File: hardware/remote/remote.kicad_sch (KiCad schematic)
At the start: 27 parts

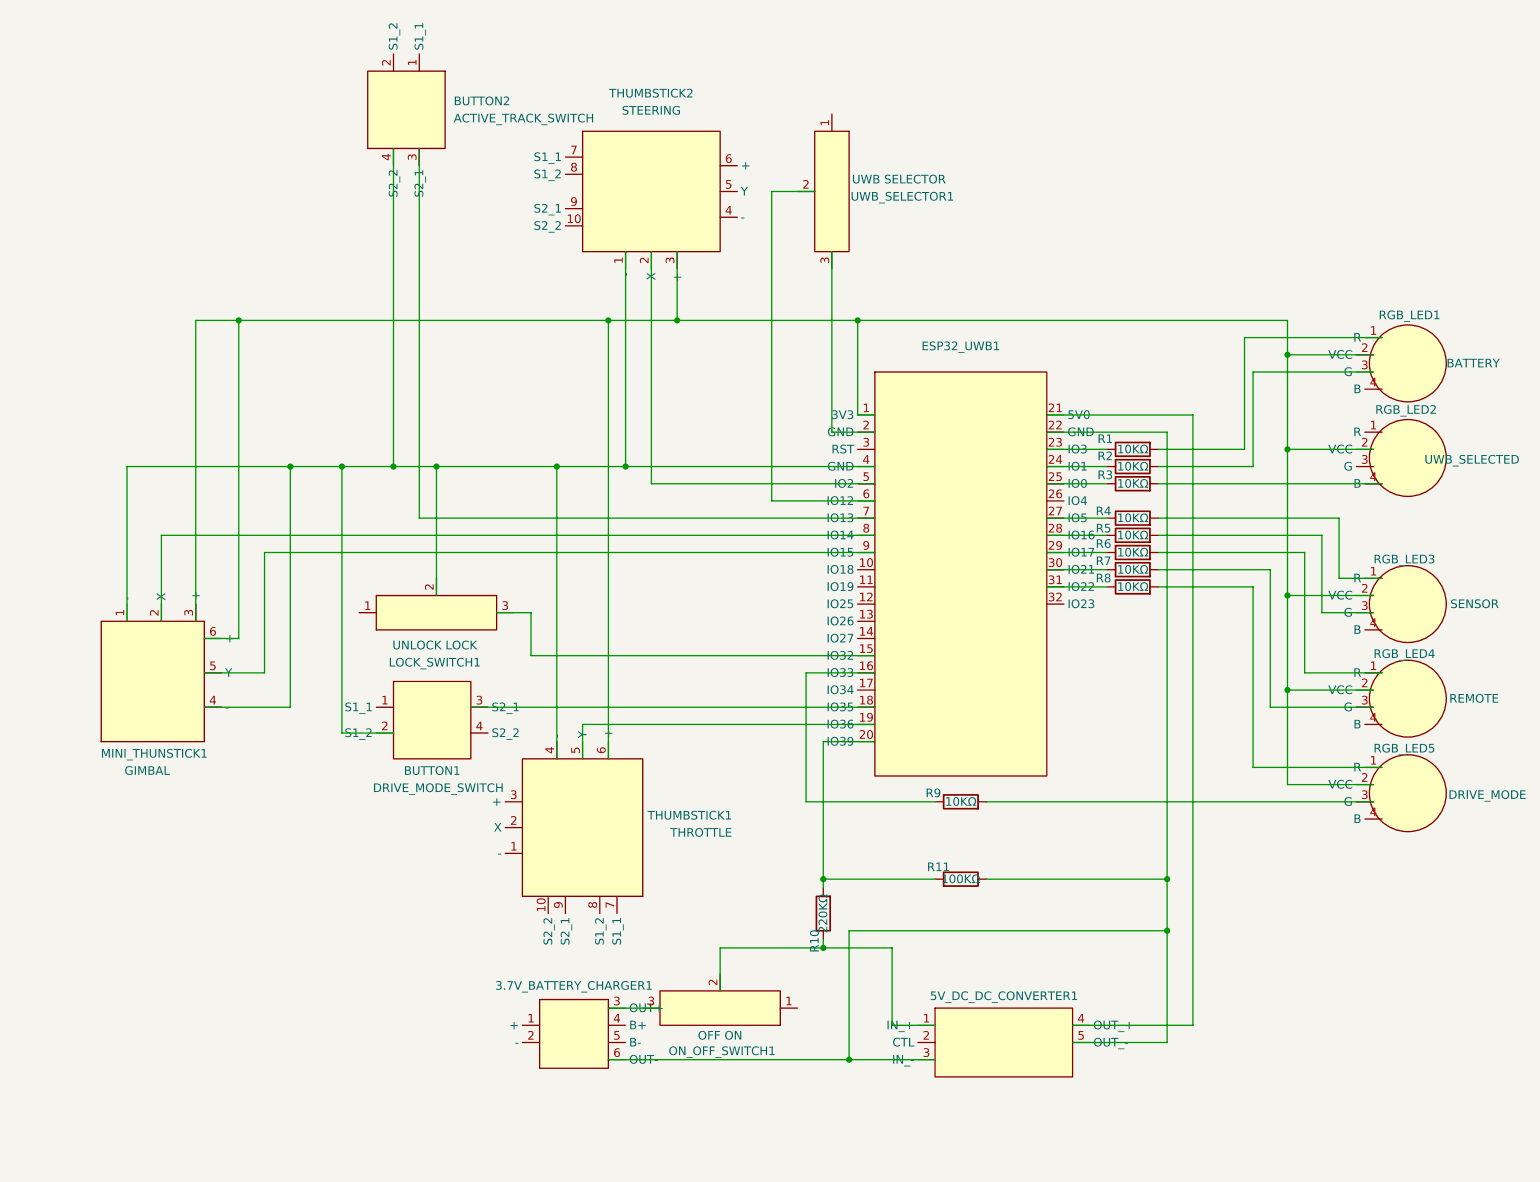
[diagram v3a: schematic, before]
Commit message: hardware: Reroute the wires to fix unavailable PINs.
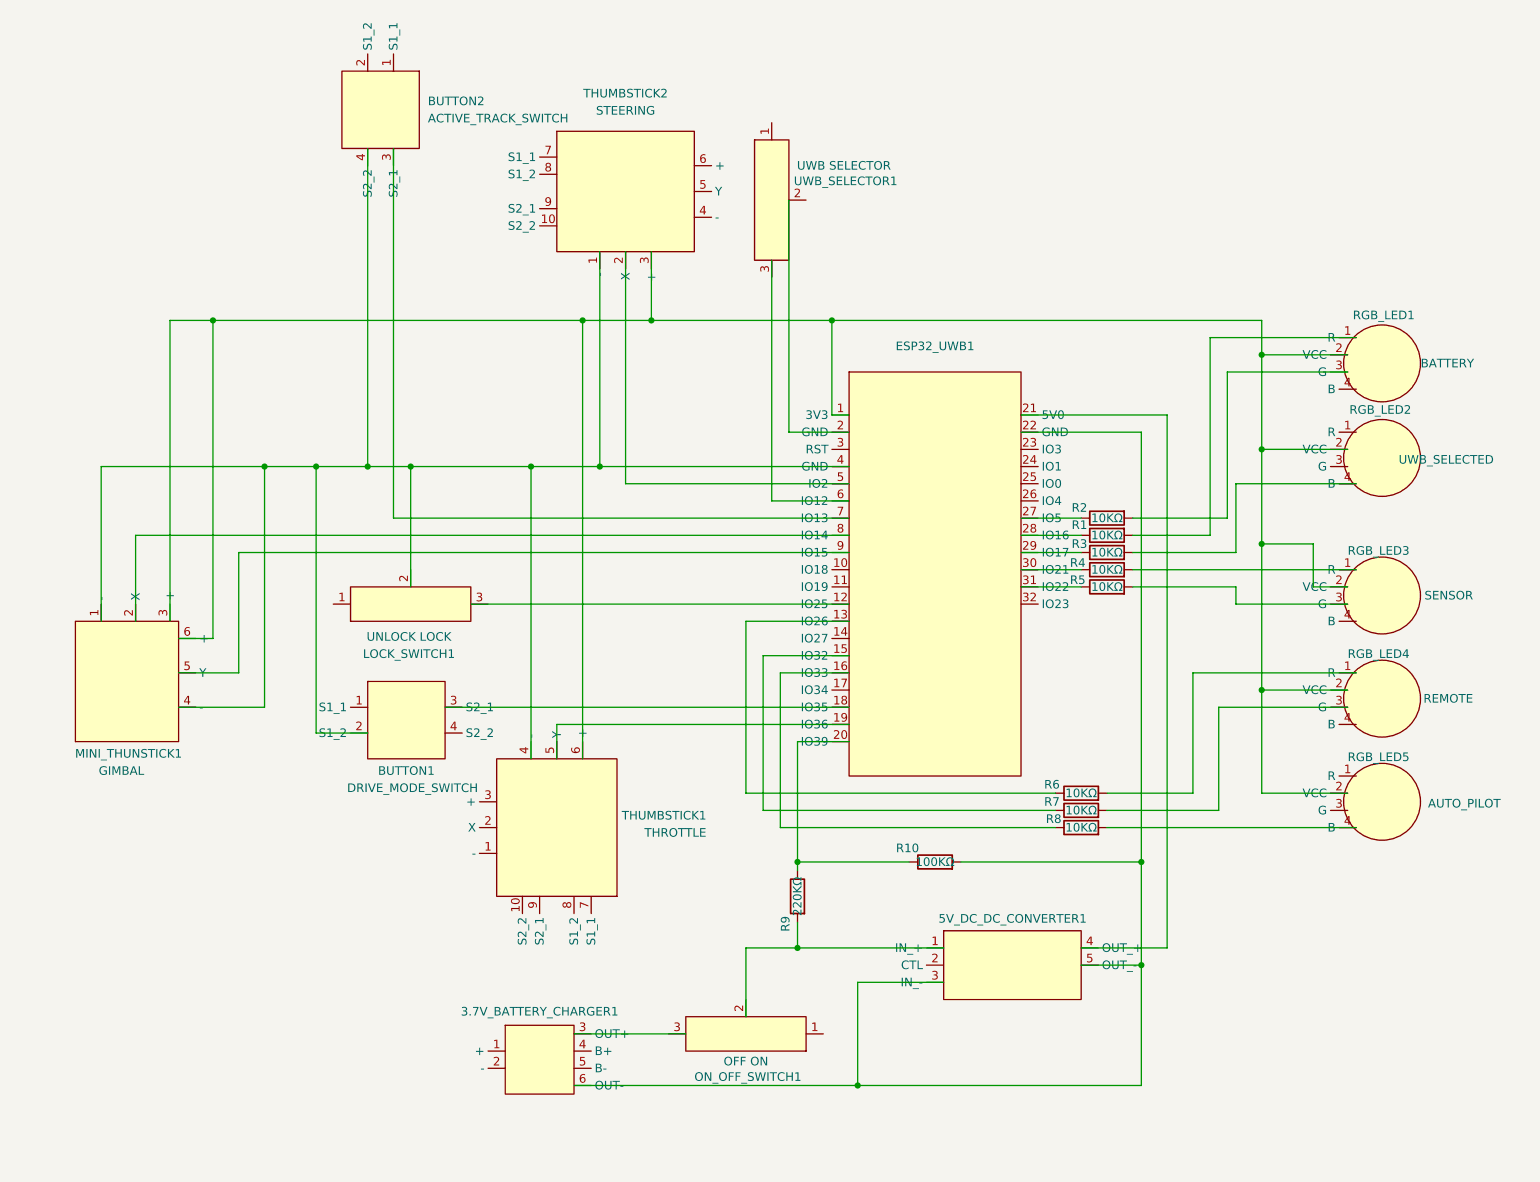
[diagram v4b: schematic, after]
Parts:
- removed R8: 10KΩ, Autocam:Simple Resistor, symbol Autocam:Simple Resistor
- RGB_LED5: value DRIVE_MODE -> AUTO_PILOT
- renumbered R11 to R10, R7 to R6, R6 to R7, R9 to R8, R10 to R9
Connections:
- net at 3.7V_BATTERY_CHARGER1.6 (OUT-), 5V_DC_DC_CONVERTER1.3 (IN_-), 5V_DC_DC_CONVERTER1.5 (OUT_-)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: now also R10.2; no longer R10.1
- net at 5V_DC_DC_CONVERTER1.1 (IN_+), ON_OFF_SWITCH1.2: now also R9.2; no longer R9.1
- net at R3.1: now also ESP32_UWB1.29 (IO17); no longer ESP32_UWB1.25 (IO0)
- net at R2.1: now also ESP32_UWB1.27 (IO5); no longer ESP32_UWB1.24 (IO1)
- net at ESP32_UWB1.31 (IO22): now also R5.1
- net at R8.2: now also RGB_LED5.4 (B); no longer RGB_LED5.3 (G)
- net at ESP32_UWB1.12 (IO25): now also LOCK_SWITCH1.3
- net at ESP32_UWB1.13 (IO26): now also R6.1
- net at ESP32_UWB1.15 (IO32): now also R7.1; no longer LOCK_SWITCH1.3
- net at ESP32_UWB1.2 (GND): now also UWB_SELECTOR1.2; no longer UWB_SELECTOR1.3
- net at ESP32_UWB1.23 (IO3): no longer R1.1
- net at R4.1: now also ESP32_UWB1.30 (IO21); no longer ESP32_UWB1.27 (IO5)
- net at ESP32_UWB1.28 (IO16): now also R1.1; no longer R5.1
- net at ESP32_UWB1.6 (IO12): now also UWB_SELECTOR1.3; no longer UWB_SELECTOR1.2
- net at RGB_LED4.1 (R): now also R6.2; no longer R7.2
- net at RGB_LED4.3 (G): now also R7.2; no longer R6.2
- new net: ESP32_UWB1.20 (IO39), R10.1, R9.1
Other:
- moved on the sheet: 3.7V_BATTERY_CHARGER1, 5V_DC_DC_CONVERTER1, BUTTON1, BUTTON2, ESP32_UWB1, LOCK_SWITCH1, MINI_THUNSTICK1, ON_OFF_SWITCH1, R1, R10, R2, R3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

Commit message: hardware: Test all the input/output pins.
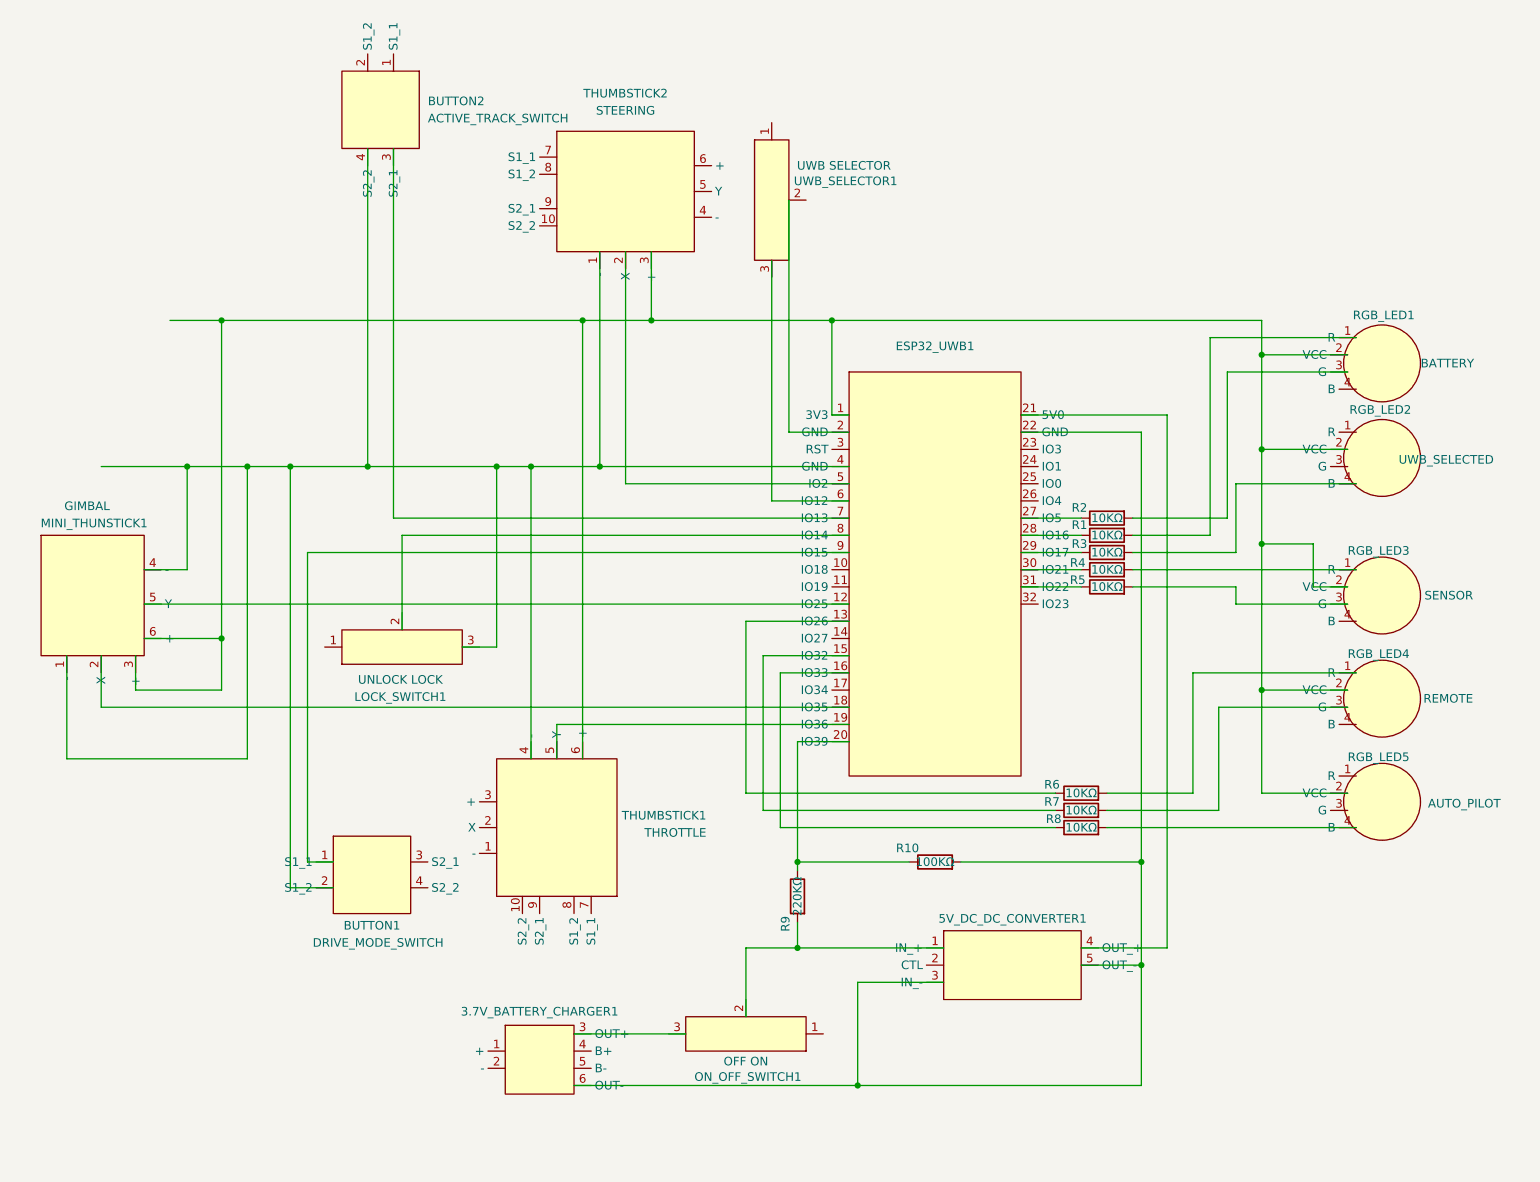
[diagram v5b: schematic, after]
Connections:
- net at BUTTON1.2 (S1_2), BUTTON2.4 (S2_2), ESP32_UWB1.4 (GND)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: now also LOCK_SWITCH1.3; no longer LOCK_SWITCH1.2
- net at BUTTON1.1 (S1_1): now also ESP32_UWB1.9 (IO15)
- net at BUTTON1.3 (S2_1): no longer ESP32_UWB1.18 (IO35)
- net at ESP32_UWB1.12 (IO25): now also MINI_THUNSTICK1.5 (Y); no longer LOCK_SWITCH1.3
- net at MINI_THUNSTICK1.2 (X): now also ESP32_UWB1.18 (IO35); no longer ESP32_UWB1.8 (IO14)
- new net: ESP32_UWB1.8 (IO14), LOCK_SWITCH1.2
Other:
- moved on the sheet: BUTTON1, LOCK_SWITCH1, MINI_THUNSTICK1

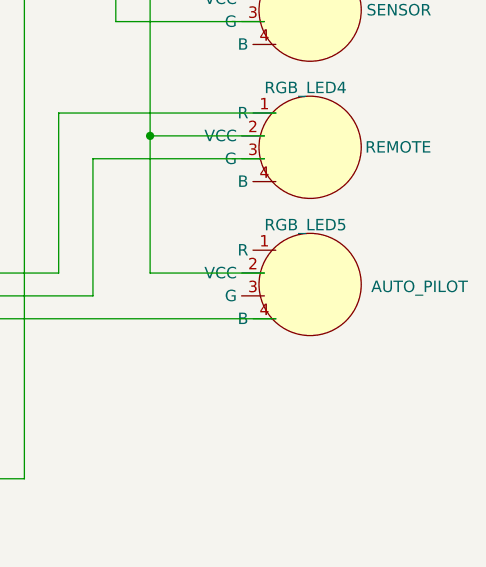
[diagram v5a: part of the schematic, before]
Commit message: hardware: Revise the drive mode naming.
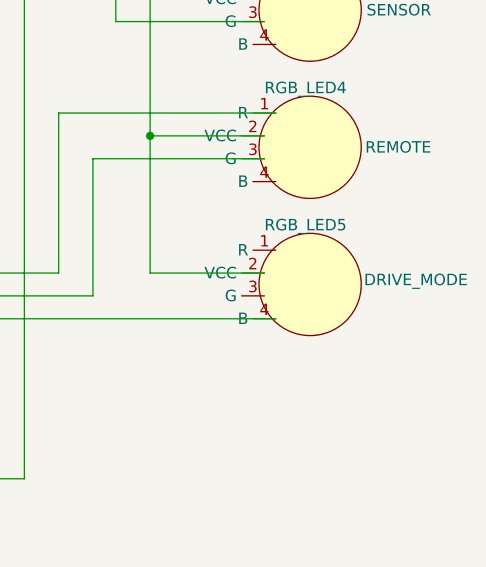
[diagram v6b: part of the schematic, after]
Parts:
- RGB_LED5: value AUTO_PILOT -> DRIVE_MODE
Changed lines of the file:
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@@
 			)
 		)
-		(property "Value" "AUTO_PILOT"
-			(at 234.696 129.794 0)
+		(property "Value" "DRIVE_MODE"
+			(at 234.696 129.032 0)
 			(effects
 				(font

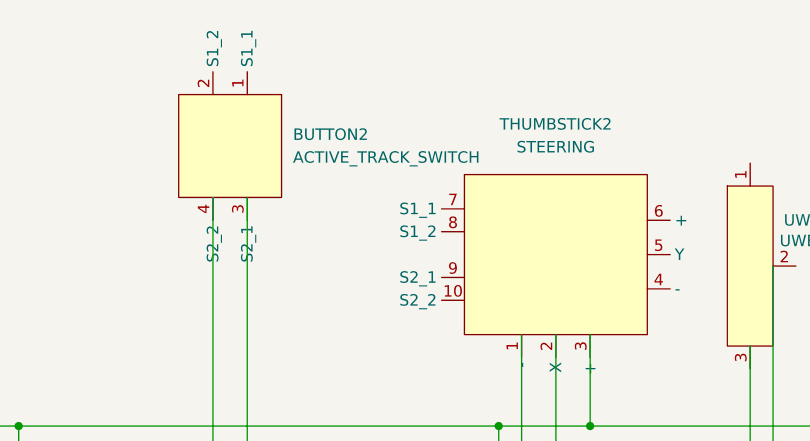
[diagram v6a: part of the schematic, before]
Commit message: hardware: Update remote gimbal fn button naming.
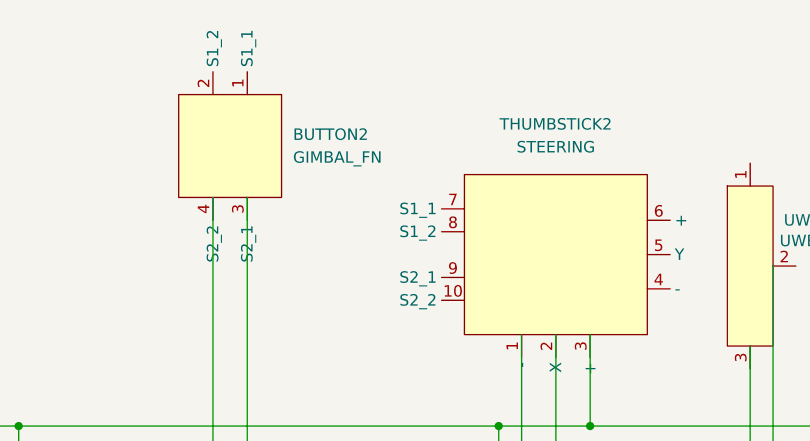
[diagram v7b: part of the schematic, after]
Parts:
- BUTTON2: value ACTIVE_TRACK_SWITCH -> GIMBAL_FN
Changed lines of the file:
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@@
 			)
 		)
-		(property "Value" "ACTIVE_TRACK_SWITCH"
+		(property "Value" "GIMBAL_FN"
 			(at 76.2 28.5749 90)
 			(effects
